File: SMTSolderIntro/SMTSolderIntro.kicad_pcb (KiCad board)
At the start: 2 copper layers, 129 parts, among them J1 USB_C_PWR_THRU, U1 NE556, U2 M74LCX04, U3 NE556

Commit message: fixed nets and components with bad footprints.  Ready for checking with printer.
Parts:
- D21, D22, D31, D32, D33, D34, D35, D36, D37, D38: footprint Diode_SMD:D_MiniMELF_Handsoldering -> Alpenglow:MINI_MELF
- D23, D24, D25, D26, D27, D28, D29, D30: footprint Diode_SMD:D_SOD-323_HandSoldering -> Alpenglow:SOD-323
- U2: footprint Alpenglow:SO-16 -> Alpenglow:SO-14
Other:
- board outline added: 88.9 x 63.5 mm

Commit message: Rough placement, added zip files to ignore
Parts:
- added D23: DIODE, Alpenglow:SOD-323, B.Cu at (127.0, 106.0)
- added D24: DIODE, Alpenglow:SOD-323, B.Cu at (191.0, 49.5)
- added D25: DIODE, Alpenglow:SOD-323, B.Cu at (191.8, 58.4)
- added D26: DIODE, Alpenglow:SOD-323, B.Cu at (131.8, 66.0)
- added H1: MountingHole_Pad, Alpenglow:MNTG-HOLE-BANANA, F.Cu at (118.1, 48.3)
- added H2: MountingHole_Pad, Alpenglow:MNTG-HOLE-BANANA, F.Cu at (199.4, 104.1)
- added H3: MountingHole_Pad, Alpenglow:MNTG-HOLE-BANANA, F.Cu at (118.1, 104.1)
- added H4: MountingHole_Pad, Alpenglow:MNTG-HOLE-BANANA, F.Cu at (199.4, 48.3)
- added J2: Barrel_Jack, Connector_BarrelJack:BarrelJack_CLIFF_FC681465S_SMT_Horizontal, B.Cu at (122.3, 61.6)
- C1, C10, C11, C12, C13, C14, C15, C16, C17, C18, C19, C2, C20, C21, C22, C23, C24, C25, C26, C27, C28, C29, C3, C30, C31, C32, C33, C34, C35, C4, C5, C6, C7, C8, C9, J1, R21, R22, R23, R24, R25, R26, R27, R28, R29, R30, R31, R32, R33, R34, R35, R36, R37, R38, R39, R40, R41, R42, R43, R44, R45, R46, R47, R48, R49, R50, R51, R52, U1, U2, U3: moved to B.Cu
- D21, D22: footprint Alpenglow:MINI_MELF -> Alpenglow:SOD-323; moved to B.Cu
- D27: renamed from D23; moved to B.Cu
- D28: renamed from D24; moved to B.Cu
- D29: renamed from D25; moved to B.Cu
- D30: renamed from D26; moved to B.Cu
- D31: renamed from D27; moved to B.Cu
- D32: renamed from D28; moved to B.Cu
- D33: renamed from D29; moved to B.Cu
- D34: renamed from D30; moved to B.Cu
- D35: renamed from D31; moved to B.Cu
- D36: renamed from D32; moved to B.Cu
- D37: renamed from D33; moved to B.Cu
- D38: renamed from D34; moved to B.Cu
- D39: renamed from D35; moved to B.Cu
- D40: renamed from D36; moved to B.Cu
- D41: renamed from D37; moved to B.Cu
- D42: renamed from D38; moved to B.Cu
- moved J1 169.1 mm to (200.7, 60.3), turned to -90 degrees
- moved C19 161.2 mm to (199.4, 98.4), turned to 180 degrees
- moved C12 159.8 mm to (199.4, 71.8), turned to 180 degrees
- moved C14 159.7 mm to (199.4, 79.4), turned to 180 degrees
- moved C17 150.6 mm to (199.4, 90.8), turned to 180 degrees
- moved R36 147.5 mm to (190.9, 106.0), turned to 180 degrees
- moved R30 145.3 mm to (190.9, 83.2), turned to 180 degrees
- moved R35 142.0 mm to (190.9, 102.2), turned to 180 degrees
- moved C15 141.6 mm to (199.4, 83.2), turned to 180 degrees
- moved C13 140.9 mm to (199.4, 75.6), turned to 180 degrees
- moved C18 138.9 mm to (199.4, 94.6), turned to 180 degrees
- moved C16 136.3 mm to (199.4, 87.0), turned to 180 degrees
- moved U1 136.2 mm to (177.2, 60.3), turned to 180 degrees
- moved R34 135.0 mm to (190.9, 98.4), turned to 180 degrees
- moved R32 132.6 mm to (190.9, 90.8), turned to 180 degrees
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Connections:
- net Net-(D21-PadK) renamed /BLINK5
- net Net-(R1-Pad1) renamed /BLINK1
- net Net-(R10-Pad1) renamed /BLINK2
- net Net-(R13-Pad1) renamed /BLINK3
- net Net-(R17-Pad1) renamed /BLINK4
- net Net-(U1-Pad5) renamed /CLK1
- net Net-(U1-Pad9) renamed /CLK2
- net Net-(U2-Pad11) renamed /CLK3
- net Net-(U2-Pad13) renamed /CLK4
- J1 pad 1: +5V -> +Vusb

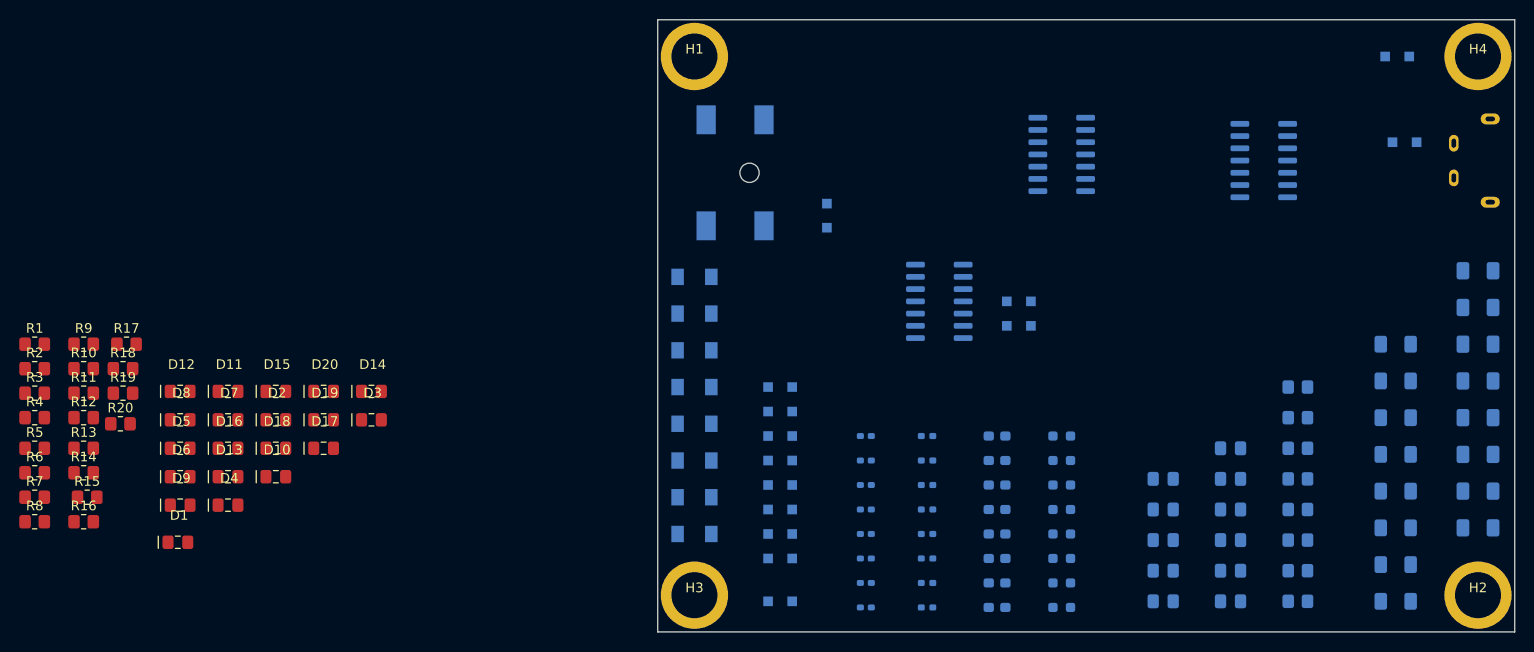
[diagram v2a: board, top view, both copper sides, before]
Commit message: finished "flower" parts placement, created sch pdf
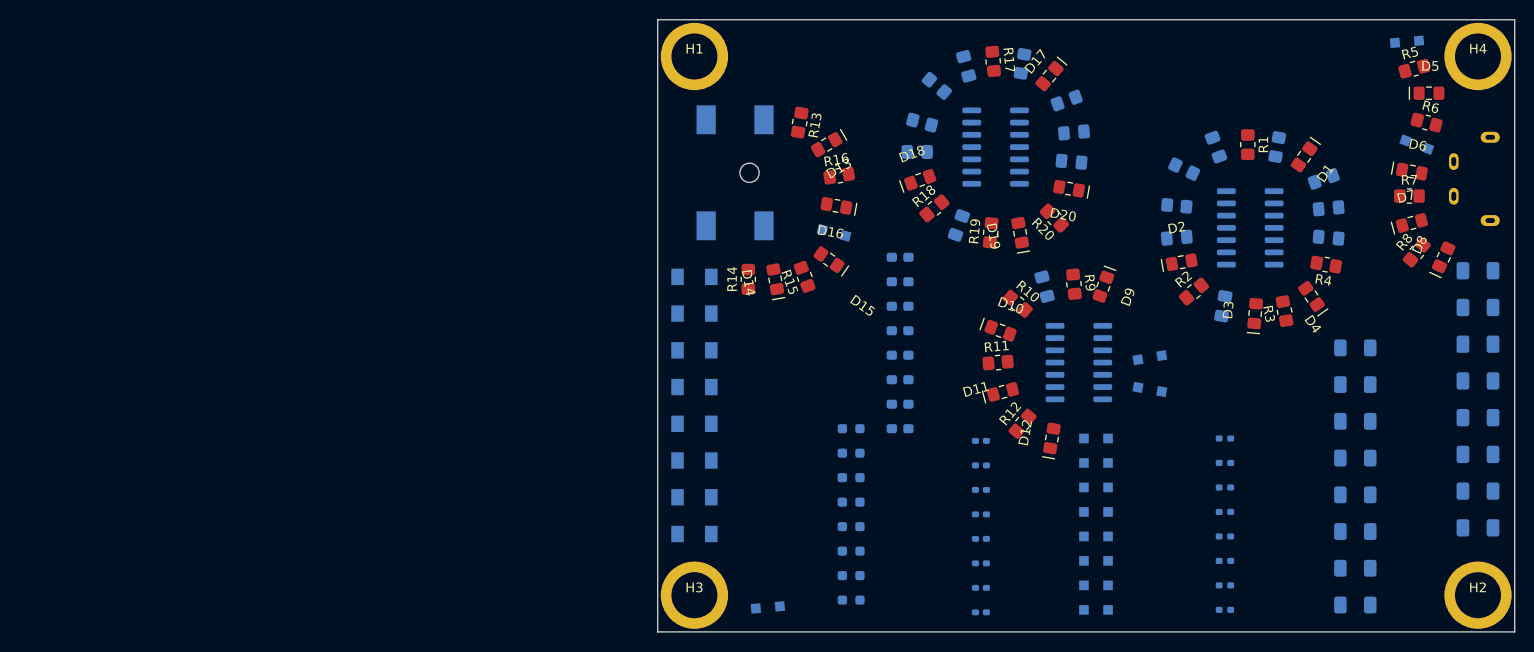
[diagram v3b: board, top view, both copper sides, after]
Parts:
- moved R6 148.9 mm to (194.1, 56.4), turned to -15 degrees
- moved R5 148.4 mm to (192.8, 50.8), turned to 15 degrees
- moved R8 146.1 mm to (193.0, 69.8), turned to 50 degrees
- moved R7 146.0 mm to (192.3, 64.0)
- moved R4 134.9 mm to (183.6, 71.1), turned to 170 degrees
- moved D5 134.7 mm to (194.3, 53.3)
- moved D8 132.1 mm to (195.8, 70.4), turned to 65 degrees
- moved D6 131.6 mm to (192.5, 61.5), turned to -10 degrees
- moved R3 129.9 mm to (179.3, 75.9), turned to 100 degrees
- moved R1 127.5 mm to (175.5, 58.7), turned to -90 degrees
- moved D7 124.5 mm to (192.5, 66.8), turned to 15 degrees
- moved D1 123.5 mm to (181.4, 59.9), turned to -125 degrees
- moved R2 120.5 mm to (169.9, 73.9), turned to 40 degrees
- moved D4 114.5 mm to (182.1, 74.4), turned to 125 degrees
- moved R9 102.9 mm to (157.5, 73.2), turned to -85 degrees
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
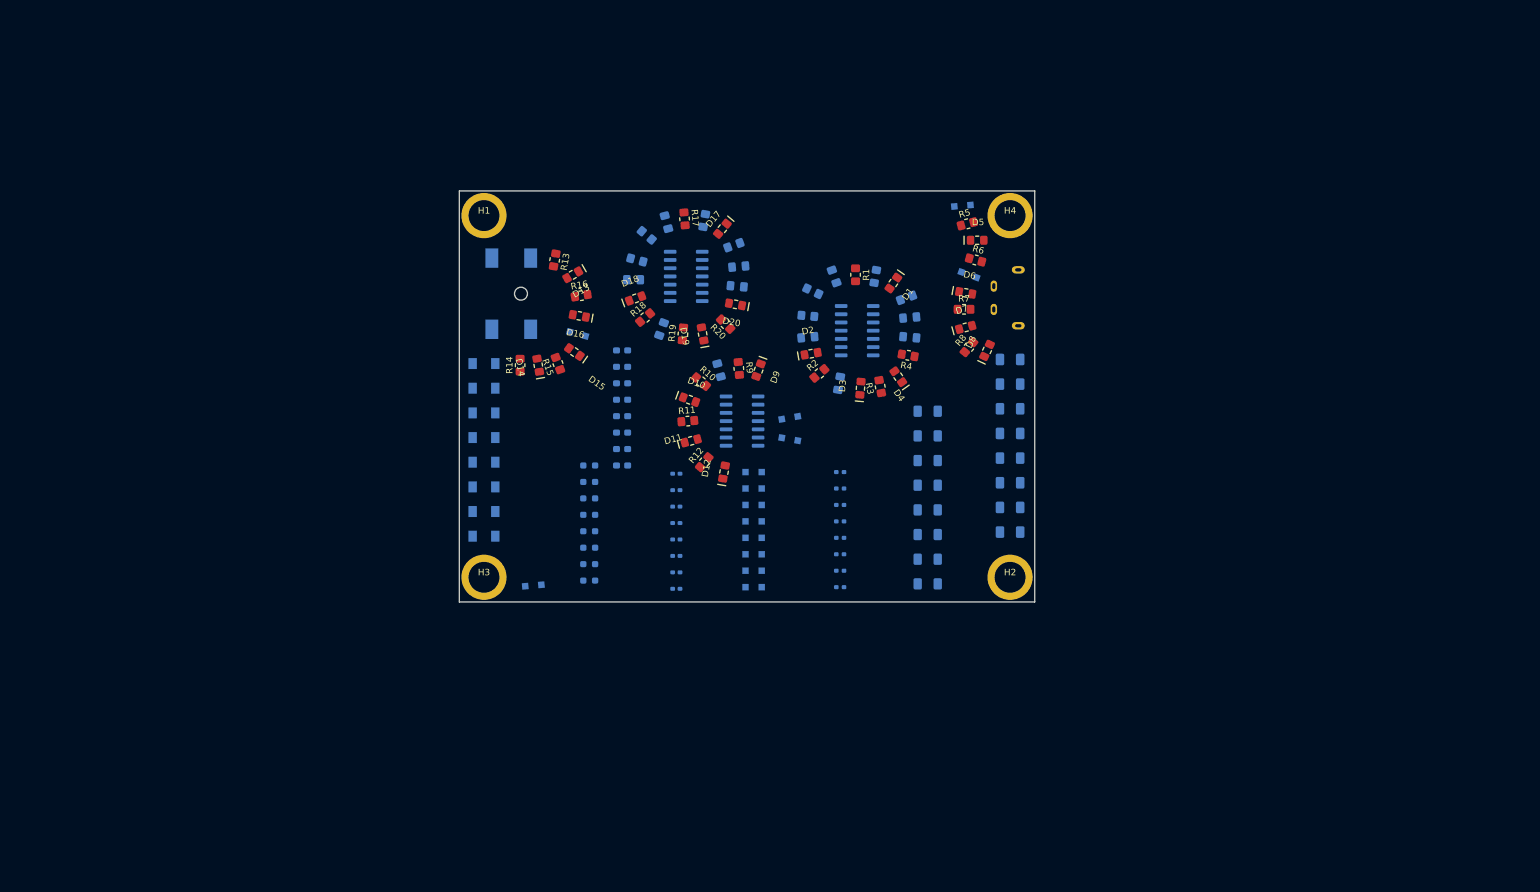
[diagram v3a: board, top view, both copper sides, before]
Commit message: Added artwork.  Started moving things around for layout
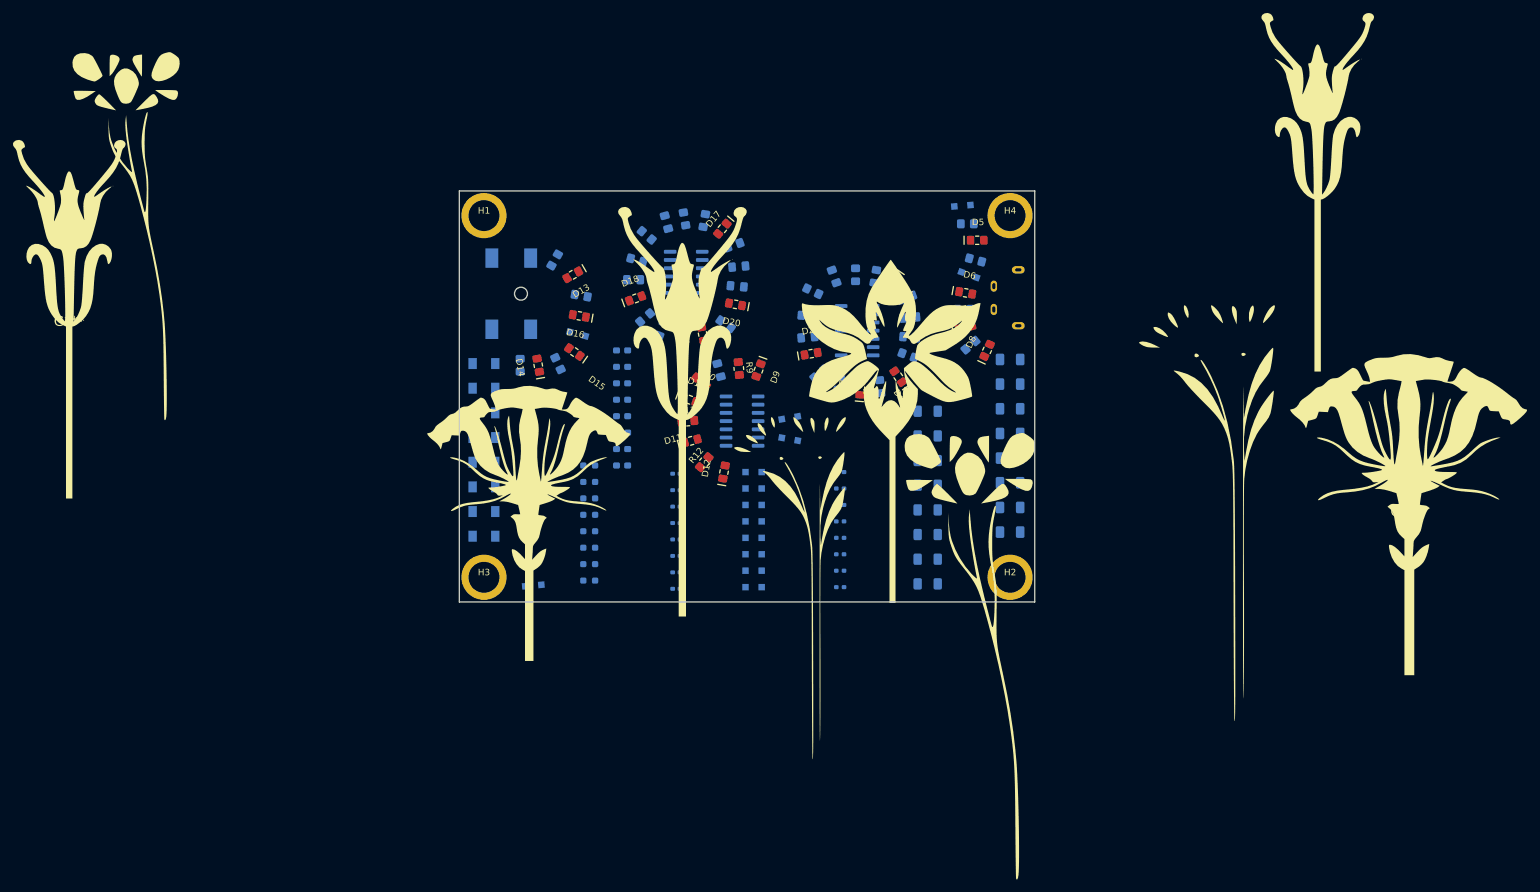
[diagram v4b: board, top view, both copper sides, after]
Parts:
- added G***: LOGO, Alpenglow_SMT_Soldering_PCB:03Inside38.9x85mm, F.Cu at (190.8, 118.8)
- added G***: LOGO, Alpenglow_SMT_Soldering_PCB:04Inside30.2x70mm, F.Cu at (167.6, 109.1)
- added G***: LOGO, Alpenglow_SMT_Soldering_PCB:04Flower30.2x70mm, F.Cu at (167.5, 108.9)
- added G***: LOGO, Alpenglow_SMT_Soldering_PCB:05Inside40.5x60mm, F.Cu at (246.9, 46.2)
- added G***: LOGO, Alpenglow_SMT_Soldering_PCB:01Flower50.3x70mm, F.Cu at (260.5, 95.2)
- added G***: LOGO, Alpenglow_SMT_Soldering_PCB:04Flower36.7x85, F.Cu at (232.3, 97.7)
- added G***: LOGO, Alpenglow_SMT_Soldering_PCB:03Inside32.1x70mm, F.Cu at (60.9, 53.8)
- added G***: LOGO, Alpenglow_SMT_Soldering_PCB:03Flower32.1x70mm, F.Cu at (60.8, 53.7)
- added G***: LOGO, Alpenglow_SMT_Soldering_PCB:04Inside36.7x85mm, F.Cu at (232.2, 97.8)
- added G***: LOGO, Alpenglow_SMT_Soldering_PCB:05Flower40.6x60mm, F.Cu at (246.9, 46.2)
- added G***: LOGO, Alpenglow_SMT_Soldering_PCB:Flower38.4x60mm, F.Cu at (180.0, 82.8)
- added G***: LOGO, Alpenglow_SMT_Soldering_PCB:01FlowerInside38.3x60mm, F.Cu at (180.0, 81.9)
- added G***: LOGO, Alpenglow_SMT_Soldering_PCB:05Flower40.6x70, F.Cu at (54.0, 65.9)
- added G***: LOGO, Alpenglow_SMT_Soldering_PCB:02Inside43x60mm, F.Cu at (124.6, 96.8)
- added G***: LOGO, Alpenglow_SMT_Soldering_PCB:02Flower43.1x60mm, F.Cu at (124.6, 96.7)
- added G***: LOGO, Alpenglow_SMT_Soldering_PCB:05Flower46.4x80mm, F.Cu at (148.8, 80.2)
- added G***: LOGO, Alpenglow_SMT_Soldering_PCB:05Inside46.3x80mm, F.Cu at (148.8, 80.1)
- added G***: LOGO, Alpenglow_SMT_Soldering_PCB:03Flower39x85mm, F.Cu at (190.7, 118.8)
- R1, R13, R14, R15, R16, R17, R18, R19, R2, R20, R3, R4, R5, R6, R7, R8: moved to B.Cu
- moved R8 0.38 mm to (193.3, 69.5), turned to 40 degrees
- turned R13 to -120 degrees
- turned R15 to 115 degrees
- turned R16 to 170 degrees
- turned R17 to -80 degrees
- turned R20 to 145 degrees
- turned R3 to 95 degrees
- turned R4 to 160 degrees
- turned R5 to 0 degrees

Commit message: Artwork layout. Saving here before moving components around
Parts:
- added G***: LOGO, Alpenglow_SMT_Soldering_PCB:01Flower44.7x70mm, F.Cu at (176.6, 78.7)
- added G***: LOGO, Alpenglow_SMT_Soldering_PCB:01Inside44.7x70mm, F.Cu at (176.6, 77.7)
- added G***: LOGO, Alpenglow_SMT_Soldering_PCB:02Flower35.9x50mm, F.Cu at (128.3, 93.2)
- added G***: LOGO, Alpenglow_SMT_Soldering_PCB:02Inside35.9x50mm, F.Cu at (128.3, 93.2)
- R10, R11, R12, R9: moved to B.Cu
- moved G*** 106.1 mm to (103.0, 154.9)
- moved G*** 106.1 mm to (103.0, 155.8)
- moved G*** 37.1 mm to (88.2, 103.8)
- moved G*** 37.1 mm to (88.2, 103.7)
- moved G*** 32.5 mm to (158.8, 113.1)
- moved G*** 32.5 mm to (158.7, 113.1)
- moved G*** 24.9 mm to (192.4, 110.0)
- moved G*** 24.9 mm to (192.5, 110.2)
- moved G*** 2.77 mm to (146.0, 80.1)
- moved G*** 2.77 mm to (146.0, 80.0)
- turned R10 to -50 degrees
- turned R11 to -5 degrees
- turned R12 to 40 degrees
- turned R9 to -95 degrees

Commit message: Fisrt Draft of artwork and component layout
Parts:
- removed the G*** at (192.5, 110.2)
- removed the G*** at (192.4, 110.0)
- removed the G*** at (246.9, 46.2) (x2)
- removed the G*** at (260.5, 95.2)
- removed the G*** at (232.3, 97.7)
- removed the G*** at (60.9, 53.8)
- removed the G*** at (60.8, 53.7)
- removed the G*** at (232.2, 97.8)
- removed the G*** at (54.0, 65.9)
- added G***: LOGO, Alpenglow_SMT_Soldering_PCB:04Flower30x70myExport, F.Cu at (192.5, 106.2)
- added G***: LOGO, Alpenglow_SMT_Soldering_PCB:04Inside30x70myExport, F.Cu at (192.5, 106.5)
- C6, D25, D26, R10, R11, R12, R13, R14, R15, R16, R6, R7, R8, R9: moved to F.Cu
- moved G*** 84.2 mm to (38.2, 102.0)
- moved G*** 84.2 mm to (38.2, 101.1)
- moved G*** 79.5 mm to (36.5, 43.3)
- moved G*** 79.5 mm to (36.5, 43.2)
- moved D24 58.9 mm to (184.7, 106.4), turned to 180 degrees
- moved R5 53.1 mm to (184.6, 103.2), turned to 180 degrees
- moved D5 52.8 mm to (191.2, 106.0), turned to 180 degrees
- moved R6 46.7 mm to (191.0, 102.9), turned to 180 degrees
- moved D25 41.3 mm to (190.8, 99.9), turned to 0 degrees
- moved D6 35.6 mm to (189.8, 97.0), turned to 180 degrees
- moved R7 30.6 mm to (188.9, 94.5), turned to 180 degrees
- moved R13 29.5 mm to (117.6, 83.5), turned to -47 degrees
- moved D3 27.2 mm to (187.3, 51.3), turned to 165 degrees
- moved R3 26.0 mm to (187.4, 51.2), turned to 165 degrees
- moved D13 25.8 mm to (120.2, 81.7), turned to -57 degrees
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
